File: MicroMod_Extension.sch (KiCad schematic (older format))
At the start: 78 parts, among them J1 2199230-4, J2 XKB_U262-16XN-4BVC11, J3 RSP-122811-01, J4 Screw_Terminal_01x04, J5 Conn_01x08, J6 Conn_01x08, J7 Conn_01x02, J8 Conn_01x04, J9 Conn_01x04, SW1 TL1014BF160QG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

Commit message: update pcb
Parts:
- removed J7: Conn_01x02, Connector_PinHeader_2.54mm:PinHeader_1x02_P2.54mm_Vertical, symbol Connector_Generic:Conn_01x02
- added J7: Conn_01x04, Connector_JST:JST_SUR_SM04B-SURS-TF_1x04-1MP_P0.80mm_Horizontal, symbol Connector_Generic:Conn_01x04
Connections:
- net GND: now also J7.4 (Pin_4)
- net NRF_TX2: now reaches U2.17 (P0.11)
- net NRF_TX2: now also J7.3 (Pin_3)
- net NRF_RX2: now reaches U2.18 (P0.12)
- net NRF_RX2: now also J7.2 (Pin_2)
- no-connect marks 41 -> 40
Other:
- moved on the sheet: J4, J6, J8, J9
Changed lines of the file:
@@
 Wire Wire Line
 	11250 5325 11250 5225
-NoConn ~ 12050 3025
-NoConn ~ 12050 3125
 NoConn ~ 12050 2725
 NoConn ~ 12050 2825
@@
 $EndComp
 $Comp
-L Connector:Screw_Terminal_01x04 J4
-U 1 1 6180CF84
-P 15425 5275
-F 0 "J4" H 15505 5267 50  0000 L CNN
-F 1 "Screw_Terminal_01x04" H 15505 5176 50  0000 L CNN
-F 2 "Connector_JST:JST_SUR_SM04B-SURS-TF_1x04-1MP_P0.80mm_Horizontal" H 15425 5275 50  0001 C CNN
-F 3 "~" H 15425 5275 50  0001 C CNN
-	1    15425 5275
-	1    0    0    -1
-$EndComp
-Text Label 15225 5275 2    50   ~ 0
-NRF_SWCLK
-Text Label 15225 5375 2    50   ~ 0
-NRF_SWIO
-Text Label 15225 5175 2    50   ~ 0
-VCC_NRF
-$Comp
-L power:GND #PWR0133
-U 1 1 61871AB2
-P 15225 5475
-F 0 "#PWR0133" H 15225 5225 50  0001 C CNN
-F 1 "GND" V 15230 5347 50  0000 R CNN
-F 2 "" H 15225 5475 50  0001 C CNN
-F 3 "" H 15225 5475 50  0001 C CNN
-	1    15225 5475
-	0    1    1    0
-$EndComp
-$Comp
-L Connector_Generic:Conn_01x02 J7
-U 1 1 6189B41D
-P 15400 750
-F 0 "J7" H 15480 742 50  0000 L CNN
-F 1 "Conn_01x02" H 15480 651 50  0000 L CNN
-F 2 "Connector_PinHeader_2.54mm:PinHeader_1x02_P2.54mm_Vertical" H 15400 750 50  0001 C CNN
-F 3 "~" H 15400 750 50  0001 C CNN
-	1    15400 750
-	1    0    0    -1
-$EndComp
-$Comp
-L power:GND #PWR0134
-U 1 1 6189BE51
-P 15200 850
-F 0 "#PWR0134" H 15200 600 50  0001 C CNN
-F 1 "GND" V 15205 722 50  0000 R CNN
-F 2 "" H 15200 850 50  0001 C CNN
-F 3 "" H 15200 850 50  0001 C CNN
-	1    15200 850
-	0    1    1    0
-$EndComp
-Text GLabel 15200 750  0    50   Input ~ 0
-BATT
-$Comp
 L Connector_Generic:Conn_01x08 J5
 U 1 1 6197BE2D
@@
 L Connector_Generic:Conn_01x08 J6
 U 1 1 6197CCB9
-P 15425 3025
-F 0 "J6" H 15505 3017 50  0000 L CNN
-F 1 "Conn_01x08" H 15505 2926 50  0000 L CNN
-F 2 "Connector_JST:JST_SUR_BM08B-SURS-TF_1x08-1MP_P0.80mm_Vertical" H 15425 3025 50  0001 C CNN
-F 3 "~" H 15425 3025 50  0001 C CNN
-	1    15425 3025
-	1    0    0    -1
-$EndComp
-Text Label 15225 2725 2    50   ~ 0
+P 14325 2000
+F 0 "J6" H 14405 1992 50  0000 L CNN
+F 1 "Conn_01x08" H 14405 1901 50  0000 L CNN
+F 2 "Connector_JST:JST_SUR_BM08B-SURS-TF_1x08-1MP_P0.80mm_Vertical" H 14325 2000 50  0001 C CNN
+F 3 "~" H 14325 2000 50  0001 C CNN
+	1    14325 2000
+	1    0    0    -1
+$EndComp
+Text Label 14125 1700 2    50   ~ 0
 VCC
 $Comp
@@
 L power:GND #PWR0136
 U 1 1 61A085B5
-P 15225 3425
-F 0 "#PWR0136" H 15225 3175 50  0001 C CNN
-F 1 "GND" V 15230 3297 50  0000 R CNN
-F 2 "" H 15225 3425 50  0001 C CNN
-F 3 "" H 15225 3425 50  0001 C CNN
-	1    15225 3425
+P 14125 2400
+F 0 "#PWR0136" H 14125 2150 50  0001 C CNN
+F 1 "GND" V 14130 2272 50  0000 R CNN
+F 2 "" H 14125 2400 50  0001 C CNN
+F 3 "" H 14125 2400 50  0001 C CNN
+	1    14125 2400
 	0    1    1    0
 $EndComp
@@
 Text Label 15225 2175 2    50   ~ 0
 MOTOR4
-Text Label 15225 2825 2    50   ~ 0
+Text Label 14125 1800 2    50   ~ 0
 E_SDA
-Text Label 15225 2925 2    50   ~ 0
+Text Label 14125 1900 2    50   ~ 0
 E_SCL
-Text Label 15225 3025 2    50   ~ 0
+Text Label 14125 2000 2    50   ~ 0
 E_SPI_SCK
-Text Label 15225 3125 2    50   ~ 0
+Text Label 14125 2100 2    50   ~ 0
 E_SPI_MISO
-Text Label 15225 3225 2    50   ~ 0
+Text Label 14125 2200 2    50   ~ 0
 E_SPI_MOSI
-Text Label 15225 3325 2    50   ~ 0
+Text Label 14125 2300 2    50   ~ 0
 B4
 Text GLabel 15225 1675 0    50   Input ~ 0
@@
 	0    1    1    0
 $EndComp
-$Comp
-L Connector_Generic:Conn_01x04 J8
-U 1 1 61BEF3FE
-P 15425 3975
-F 0 "J8" H 15505 3967 50  0000 L CNN
-F 1 "Conn_01x04" H 15505 3876 50  0000 L CNN
-F 2 "Connector_JST:JST_SUR_SM04B-SURS-TF_1x04-1MP_P0.80mm_Horizontal" H 15425 3975 50  0001 C CNN
-F 3 "~" H 15425 3975 50  0001 C CNN
-	1    15425 3975
-	1    0    0    -1
-$EndComp
-$Comp
-L power:GND #PWR0138
-U 1 1 61BF109A
-P 15225 4175
-F 0 "#PWR0138" H 15225 3925 50  0001 C CNN
-F 1 "GND" V 15230 4047 50  0000 R CNN
-F 2 "" H 15225 4175 50  0001 C CNN
-F 3 "" H 15225 4175 50  0001 C CNN
-	1    15225 4175
-	0    1    1    0
-$EndComp
-Text Label 15225 3975 2    50   ~ 0
-E_RX1
-Text Label 15225 4075 2    50   ~ 0
-E_TX1
-$Comp
-L Connector_Generic:Conn_01x04 J9
-U 1 1 61C420AB
-P 15425 4625
-F 0 "J9" H 15505 4617 50  0000 L CNN
-F 1 "Conn_01x04" H 15505 4526 50  0000 L CNN
-F 2 "Connector_JST:JST_SUR_SM04B-SURS-TF_1x04-1MP_P0.80mm_Horizontal" H 15425 4625 50  0001 C CNN
-F 3 "~" H 15425 4625 50  0001 C CNN
-	1    15425 4625
-	1    0    0    -1
-$EndComp
-$Comp
-L power:GND #PWR0139
-U 1 1 61C420B1
-P 15225 4825
-F 0 "#PWR0139" H 15225 4575 50  0001 C CNN
-F 1 "GND" V 15230 4697 50  0000 R CNN
-F 2 "" H 15225 4825 50  0001 C CNN
-F 3 "" H 15225 4825 50  0001 C CNN
-	1    15225 4825
-	0    1    1    0
-$EndComp
-Text Label 15225 4625 2    50   ~ 0
-E_RX2
-Text Label 15225 4725 2    50   ~ 0
-E_TX2
-Wire Notes Line
-	14700 5650 14700 475
-Wire Notes Line
-	14700 5650 16050 5650
 Text Notes 14800 600  0    50   ~ 0
 Connector
@@
 	14775 1200 14925 1200
 Connection ~ 14925 1200
-NoConn ~ 15225 3875
-NoConn ~ 15225 4525
+Text Label 12050 3025 0    50   ~ 0
+NRF_TX2
+Text Label 12050 3125 0    50   ~ 0
+NRF_RX2
+NoConn ~ 14100 2700
+Text Label 14100 2900 2    50   ~ 0
+NRF_TX2
+Text Label 14100 2800 2    50   ~ 0
+NRF_RX2
+$Comp
+L power:GND #PWR0134
+U 1 1 61889B5C
+P 14100 3000
+F 0 "#PWR0134" H 14100 2750 50  0001 C CNN
+F 1 "GND" V 14105 2872 50  0000 R CNN
+F 2 "" H 14100 3000 50  0001 C CNN
+F 3 "" H 14100 3000 50  0001 C CNN
+	1    14100 3000
+	0    1    1    0
+$EndComp
+$Comp
+L Connector_Generic:Conn_01x04 J7
+U 1 1 61889B56
+P 14300 2800
+F 0 "J7" H 14380 2792 50  0000 L CNN
+F 1 "Conn_01x04" H 14380 2701 50  0000 L CNN
+F 2 "Connector_JST:JST_SUR_SM04B-SURS-TF_1x04-1MP_P0.80mm_Horizontal" H 14300 2800 50  0001 C CNN
+F 3 "~" H 14300 2800 50  0001 C CNN
+	1    14300 2800
+	1    0    0    -1
+$EndComp
+NoConn ~ 15050 3325
+NoConn ~ 15050 2675
+Text Label 15050 3525 2    50   ~ 0
+E_TX2
+Text Label 15050 3425 2    50   ~ 0
+E_RX2
+$Comp
+L power:GND #PWR0139
+U 1 1 61C420B1
+P 15050 3625
+F 0 "#PWR0139" H 15050 3375 50  0001 C CNN
+F 1 "GND" V 15055 3497 50  0000 R CNN
+F 2 "" H 15050 3625 50  0001 C CNN
+F 3 "" H 15050 3625 50  0001 C CNN
+	1    15050 3625
+	0    1    1    0
+$EndComp
+$Comp
+L Connector_Generic:Conn_01x04 J9
+U 1 1 61C420AB
+P 15250 3425
+F 0 "J9" H 15330 3417 50  0000 L CNN
+F 1 "Conn_01x04" H 15330 3326 50  0000 L CNN
+F 2 "Connector_JST:JST_SUR_SM04B-SURS-TF_1x04-1MP_P0.80mm_Horizontal" H 15250 3425 50  0001 C CNN
+F 3 "~" H 15250 3425 50  0001 C CNN
+	1    15250 3425
+	1    0    0    -1
+$EndComp
+Text Label 15050 2875 2    50   ~ 0
+E_TX1
+Text Label 15050 2775 2    50   ~ 0
+E_RX1
+$Comp
+L power:GND #PWR0138
+U 1 1 61BF109A
+P 15050 2975
+F 0 "#PWR0138" H 15050 2725 50  0001 C CNN
+F 1 "GND" V 15055 2847 50  0000 R CNN
+F 2 "" H 15050 2975 50  0001 C CNN
+F 3 "" H 15050 2975 50  0001 C CNN
+	1    15050 2975
+	0    1    1    0
+$EndComp
+$Comp
+L Connector_Generic:Conn_01x04 J8
+U 1 1 61BEF3FE
+P 15250 2775
+F 0 "J8" H 15330 2767 50  0000 L CNN
+F 1 "Conn_01x04" H 15330 2676 50  0000 L CNN
+F 2 "Connector_JST:JST_SUR_SM04B-SURS-TF_1x04-1MP_P0.80mm_Horizontal" H 15250 2775 50  0001 C CNN
+F 3 "~" H 15250 2775 50  0001 C CNN
+	1    15250 2775
+	1    0    0    -1
+$EndComp
+$Comp
+L power:GND #PWR0133
+U 1 1 61871AB2
+P 14125 3625
+F 0 "#PWR0133" H 14125 3375 50  0001 C CNN
+F 1 "GND" V 14130 3497 50  0000 R CNN
+F 2 "" H 14125 3625 50  0001 C CNN
+F 3 "" H 14125 3625 50  0001 C CNN
+	1    14125 3625
+	0    1    1    0
+$EndComp
+Text Label 14125 3325 2    50   ~ 0
+VCC_NRF
+Text Label 14125 3525 2    50   ~ 0
+NRF_SWIO
+Text Label 14125 3425 2    50   ~ 0
+NRF_SWCLK
+$Comp
+L Connector:Screw_Terminal_01x04 J4
+U 1 1 6180CF84
+P 14325 3425
+F 0 "J4" H 14405 3417 50  0000 L CNN
+F 1 "Screw_Terminal_01x04" H 14405 3326 50  0000 L CNN
+F 2 "Connector_JST:JST_SUR_SM04B-SURS-TF_1x04-1MP_P0.80mm_Horizontal" H 14325 3425 50  0001 C CNN
+F 3 "~" H 14325 3425 50  0001 C CNN
+	1    14325 3425
+	1    0    0    -1
+$EndComp
 $EndSCHEMATC

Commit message: finish version 1.0
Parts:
- added J10: Conn_01x02, MicroMod_Extension:BATTARY, symbol Connector_Generic:Conn_01x02
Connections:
- net BATT: now also J10.1 (Pin_1)
- net GND: now also J10.2 (Pin_2)
- net at FL2.2 (OUT/IN): now also C11.2; no longer J3.1
- net at FL3.2 (OUT/IN): now also J3.1; no longer C11.2
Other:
- moved on the sheet: C11, E1, J3, L1, L3
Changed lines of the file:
@@
 L MicroMod_Extension:RSP-122811-01 J3
 U 1 1 617ED359
-P 4200 1550
-F 0 "J3" H 4192 1857 50  0000 C CNN
-F 1 "RSP-122811-01" H 4192 1766 50  0000 C CNN
-F 2 "MicroMod_Extension:SAMTEC_RSP-122811-01" H 4200 1550 50  0001 L BNN
-F 3 "" H 4200 1550 50  0001 L BNN
-F 4 "Samtec" H 4200 1550 50  0001 L BNN "MANUFACTURER"
-F 5 "H" H 4200 1550 50  0001 L BNN "PARTREV"
-F 6 "Manufacturer Recommendations" H 4200 1550 50  0001 L BNN "STANDARD"
-F 7 "1.44mm" H 4200 1550 50  0001 L BNN "MAXIMUM_PACKAGE_HEIGHT"
-	1    4200 1550
-	1    0    0    -1
-$EndComp
-Wire Wire Line
-	4300 1450 4600 1450
+P 4200 2675
+F 0 "J3" H 4192 2982 50  0000 C CNN
+F 1 "RSP-122811-01" H 4192 2891 50  0000 C CNN
+F 2 "MicroMod_Extension:SAMTEC_RSP-122811-01" H 4200 2675 50  0001 L BNN
+F 3 "" H 4200 2675 50  0001 L BNN
+F 4 "Samtec" H 4200 2675 50  0001 L BNN "MANUFACTURER"
+F 5 "H" H 4200 2675 50  0001 L BNN "PARTREV"
+F 6 "Manufacturer Recommendations" H 4200 2675 50  0001 L BNN "STANDARD"
+F 7 "1.44mm" H 4200 2675 50  0001 L BNN "MAXIMUM_PACKAGE_HEIGHT"
+	1    4200 2675
+	1    0    0    -1
+$EndComp
+Wire Wire Line
+	4300 2575 4600 2575
 $Comp
 L power:GND #PWR0119
 U 1 1 617F3384
-P 4300 1550
-F 0 "#PWR0119" H 4300 1300 50  0001 C CNN
-F 1 "GND" V 4305 1422 50  0000 R CNN
-F 2 "" H 4300 1550 50  0001 C CNN
-F 3 "" H 4300 1550 50  0001 C CNN
-	1    4300 1550
+P 4300 2675
+F 0 "#PWR0119" H 4300 2425 50  0001 C CNN
+F 1 "GND" V 4305 2547 50  0000 R CNN
+F 2 "" H 4300 2675 50  0001 C CNN
+F 3 "" H 4300 2675 50  0001 C CNN
+	1    4300 2675
 	0    -1   -1   0
 $EndComp
@@
 L Device:C C11
 U 1 1 6180E811
-P 4450 2575
-F 0 "C11" H 4565 2621 50  0000 L CNN
-F 1 "2.5p" H 4565 2530 50  0000 L CNN
-F 2 "Capacitor_SMD:C_0402_1005Metric" H 4488 2425 50  0001 C CNN
-F 3 "~" H 4450 2575 50  0001 C CNN
-	1    4450 2575
+P 4450 1450
+F 0 "C11" H 4565 1496 50  0000 L CNN
+F 1 "2.5p" H 4565 1405 50  0000 L CNN
+F 2 "Capacitor_SMD:C_0402_1005Metric" H 4488 1300 50  0001 C CNN
+F 3 "~" H 4450 1450 50  0001 C CNN
+	1    4450 1450
 	0    -1   -1   0
 $EndComp
@@
 L Device:L L3
 U 1 1 61810D4B
-P 4200 2825
-F 0 "L3" H 4253 2871 50  0000 L CNN
-F 1 "1nH" H 4253 2780 50  0000 L CNN
-F 2 "Inductor_SMD:L_0402_1005Metric" H 4200 2825 50  0001 C CNN
-F 3 "~" H 4200 2825 50  0001 C CNN
-	1    4200 2825
+P 4200 1700
+F 0 "L3" H 4253 1746 50  0000 L CNN
+F 1 "1nH" H 4253 1655 50  0000 L CNN
+F 2 "Inductor_SMD:L_0402_1005Metric" H 4200 1700 50  0001 C CNN
+F 3 "~" H 4200 1700 50  0001 C CNN
+	1    4200 1700
 	1    0    0    -1
 $EndComp
@@
 L Device:L L1
 U 1 1 61813241
-P 3950 2575
-F 0 "L1" V 4140 2575 50  0000 C CNN
-F 1 "4.7nH" V 4049 2575 50  0000 C CNN
-F 2 "Inductor_SMD:L_0402_1005Metric" H 3950 2575 50  0001 C CNN
-F 3 "~" H 3950 2575 50  0001 C CNN
-	1    3950 2575
+P 3950 1450
+F 0 "L1" V 4140 1450 50  0000 C CNN
+F 1 "4.7nH" V 4049 1450 50  0000 C CNN
+F 2 "Inductor_SMD:L_0402_1005Metric" H 3950 1450 50  0001 C CNN
+F 3 "~" H 3950 1450 50  0001 C CNN
+	1    3950 1450
 	0    -1   -1   0
 $EndComp
 Wire Wire Line
-	4100 2575 4200 2575
-Wire Wire Line
-	4200 2575 4200 2675
-Wire Wire Line
-	4200 2575 4300 2575
-Connection ~ 4200 2575
-Wire Wire Line
-	4200 2975 4200 3075
+	4100 1450 4200 1450
+Wire Wire Line
+	4200 1450 4200 1550
+Wire Wire Line
+	4200 1450 4300 1450
+Connection ~ 4200 1450
+Wire Wire Line
+	4200 1850 4200 1950
 $Comp
 L power:GND #PWR0121
 U 1 1 6181C983
-P 4200 3075
-F 0 "#PWR0121" H 4200 2825 50  0001 C CNN
-F 1 "GND" V 4205 2947 50  0000 R CNN
-F 2 "" H 4200 3075 50  0001 C CNN
-F 3 "" H 4200 3075 50  0001 C CNN
-	1    4200 3075
+P 4200 1950
+F 0 "#PWR0121" H 4200 1700 50  0001 C CNN
+F 1 "GND" V 4205 1822 50  0000 R CNN
+F 2 "" H 4200 1950 50  0001 C CNN
+F 3 "" H 4200 1950 50  0001 C CNN
+	1    4200 1950
 	1    0    0    -1
 $EndComp
@@
 L MicroMod_Extension:2450AT18B100E E1
 U 1 1 61821C76
-P 3725 2300
-F 0 "E1" H 3850 2397 50  0000 L CNN
-F 1 "2450AT18B100E" H 3850 2306 50  0000 L CNN
-F 2 "MicroMod_Extension:XDCR_2450AT18B100E" H 3725 2300 50  0001 L BNN
-F 3 "" H 3725 2300 50  0001 L BNN
-F 4 "Manufacturer Recommendation" H 3725 2300 50  0001 L BNN "STANDARD"
-F 5 "4.0" H 3725 2300 50  0001 L BNN "PARTREV"
-F 6 "Johanson Technology" H 3725 2300 50  0001 L BNN "MANUFACTURER"
-F 7 "1.4 mm" H 3725 2300 50  0001 L BNN "MAXIMUM_PACKAGE_HEIGHT"
-	1    3725 2300
-	1    0    0    -1
-$EndComp
-Wire Wire Line
-	3725 2500 3725 2575
-Wire Wire Line
-	3725 2575 3800 2575
+P 3725 1175
+F 0 "E1" H 3850 1272 50  0000 L CNN
+F 1 "2450AT18B100E" H 3850 1181 50  0000 L CNN
+F 2 "MicroMod_Extension:XDCR_2450AT18B100E" H 3725 1175 50  0001 L BNN
+F 3 "" H 3725 1175 50  0001 L BNN
+F 4 "Manufacturer Recommendation" H 3725 1175 50  0001 L BNN "STANDARD"
+F 5 "4.0" H 3725 1175 50  0001 L BNN "PARTREV"
+F 6 "Johanson Technology" H 3725 1175 50  0001 L BNN "MANUFACTURER"
+F 7 "1.4 mm" H 3725 1175 50  0001 L BNN "MAXIMUM_PACKAGE_HEIGHT"
+	1    3725 1175
+	1    0    0    -1
+$EndComp
+Wire Wire Line
+	3725 1375 3725 1450
+Wire Wire Line
+	3725 1450 3800 1450
 Text Label 12050 3825 0    50   ~ 0
 PA_SW_ANT
@@
 	1    0    0    -1
 $EndComp
+$Comp
+L Connector_Generic:Conn_01x02 J10
+U 1 1 61893954
+P 15450 750
+F 0 "J10" H 15530 742 50  0000 L CNN
+F 1 "Conn_01x02" H 15530 651 50  0000 L CNN
+F 2 "MicroMod_Extension:BATTARY" H 15450 750 50  0001 C CNN
+F 3 "~" H 15450 750 50  0001 C CNN
+	1    15450 750
+	1    0    0    -1
+$EndComp
+$Comp
+L power:GND #PWR0141
+U 1 1 61894E7F
+P 15250 850
+F 0 "#PWR0141" H 15250 600 50  0001 C CNN
+F 1 "GND" V 15255 722 50  0000 R CNN
+F 2 "" H 15250 850 50  0001 C CNN
+F 3 "" H 15250 850 50  0001 C CNN
+	1    15250 850
+	0    1    1    0
+$EndComp
+Text GLabel 15250 750  0    50   Input ~ 0
+BATT
 $EndSCHEMATC

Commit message: update pcb
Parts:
- added J11: Screw_Terminal_01x04, Connector_JST:JST_SUR_SM04B-SURS-TF_1x04-1MP_P0.80mm_Horizontal, symbol Connector:Screw_Terminal_01x04
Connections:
- net GND: now also J11.4 (Pin_4)
- net STM_SWCLK: now also J11.2 (Pin_2)
- net STM_SWIO: now also J11.3 (Pin_3)
- net VCC: now also J11.1 (Pin_1)
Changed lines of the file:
@@
 Text GLabel 15250 750  0    50   Input ~ 0
 BATT
+$Comp
+L power:GND #PWR0142
+U 1 1 619F1B8D
+P 14125 4275
+F 0 "#PWR0142" H 14125 4025 50  0001 C CNN
+F 1 "GND" V 14130 4147 50  0000 R CNN
+F 2 "" H 14125 4275 50  0001 C CNN
+F 3 "" H 14125 4275 50  0001 C CNN
+	1    14125 4275
+	0    1    1    0
+$EndComp
+Text Label 14125 3975 2    50   ~ 0
+VCC
+Text Label 14125 4175 2    50   ~ 0
+STM_SWIO
+Text Label 14125 4075 2    50   ~ 0
+STM_SWCLK
+$Comp
+L Connector:Screw_Terminal_01x04 J11
+U 1 1 619F1B96
+P 14325 4075
+F 0 "J11" H 14405 4067 50  0000 L CNN
+F 1 "Screw_Terminal_01x04" H 14405 3976 50  0000 L CNN
+F 2 "Connector_JST:JST_SUR_SM04B-SURS-TF_1x04-1MP_P0.80mm_Horizontal" H 14325 4075 50  0001 C CNN
+F 3 "~" H 14325 4075 50  0001 C CNN
+	1    14325 4075
+	1    0    0    -1
+$EndComp
 $EndSCHEMATC

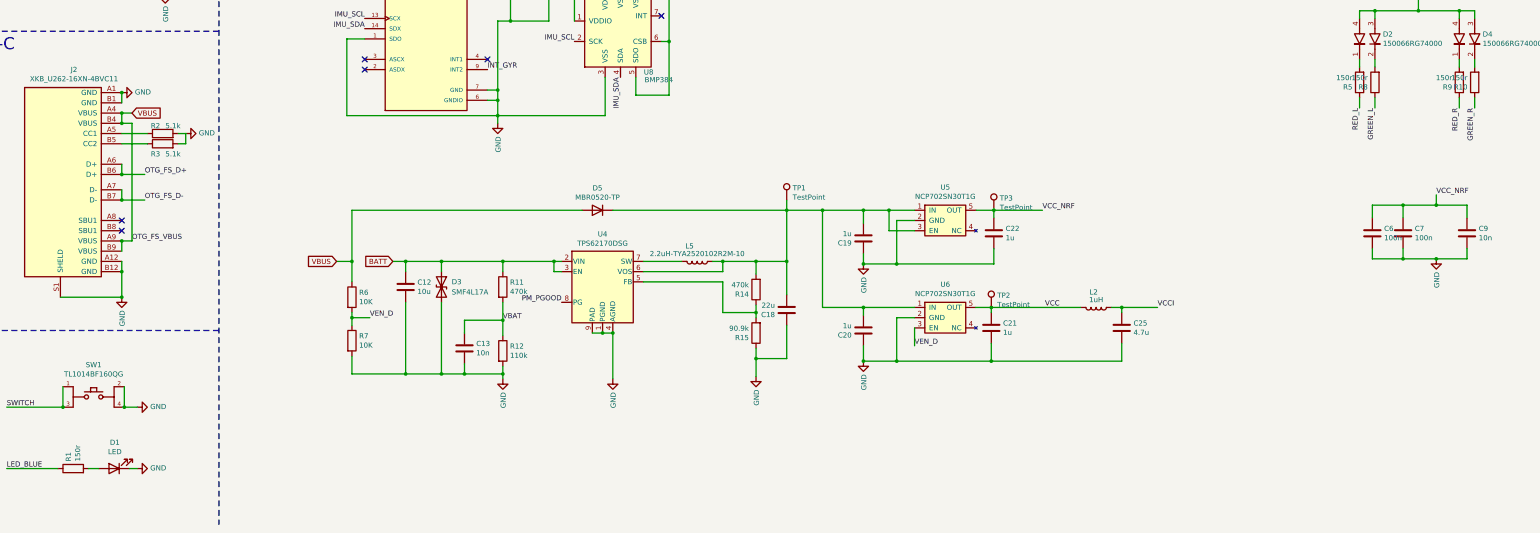
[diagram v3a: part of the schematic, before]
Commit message: fix led resistance
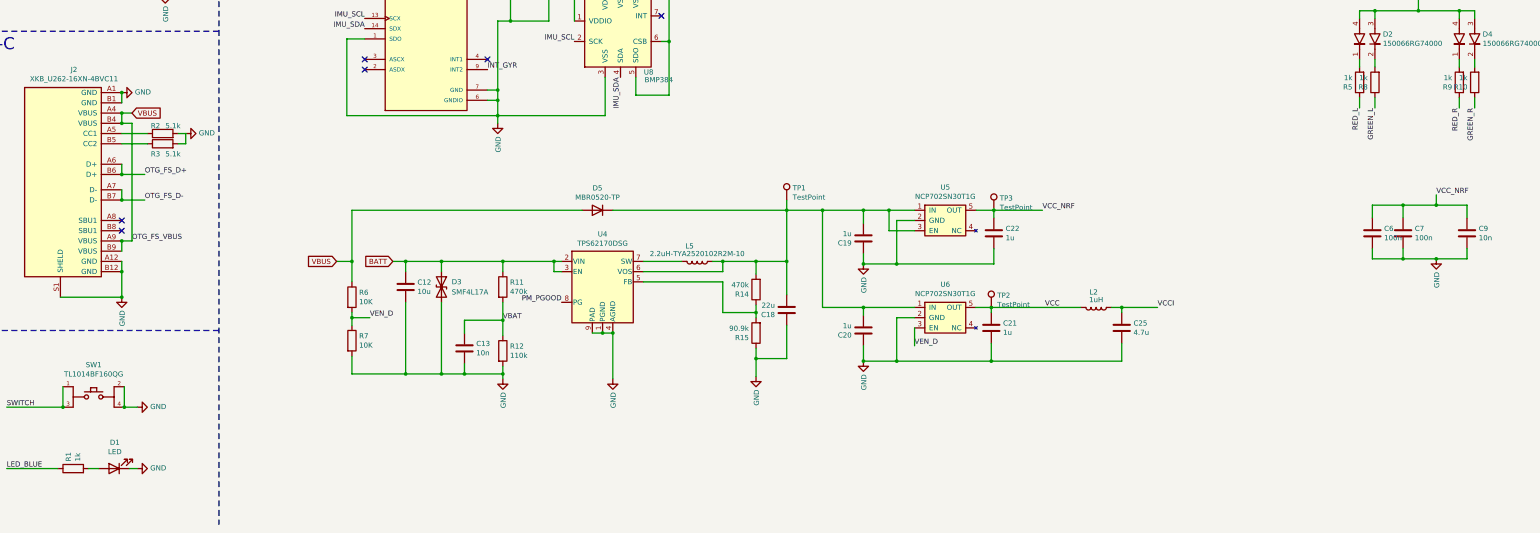
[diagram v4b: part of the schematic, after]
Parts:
- R1, R10, R5, R8, R9: value 150r -> 1k
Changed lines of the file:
@@
 P 1575 10675
 F 0 "R1" H 1645 10721 50  0000 L CNN
-F 1 "150r" H 1645 10630 50  0000 L CNN
+F 1 "1k" H 1645 10630 50  0000 L CNN
 F 2 "Resistor_SMD:R_0402_1005Metric" V 1505 10675 50  0001 C CNN
 F 3 "~" H 1575 10675 50  0001 C CNN
@@
 P 14150 6900
 F 0 "R5" H 14220 6946 50  0000 L CNN
-F 1 "150r" H 14220 6855 50  0000 L CNN
+F 1 "1k" H 14220 6855 50  0000 L CNN
 F 2 "Resistor_SMD:R_0402_1005Metric" V 14080 6900 50  0001 C CNN
 F 3 "~" H 14150 6900 50  0001 C CNN
@@
 P 14300 6900
 F 0 "R8" H 14370 6946 50  0000 L CNN
-F 1 "150r" H 14370 6855 50  0000 L CNN
+F 1 "1k" H 14370 6855 50  0000 L CNN
 F 2 "Resistor_SMD:R_0402_1005Metric" V 14230 6900 50  0001 C CNN
 F 3 "~" H 14300 6900 50  0001 C CNN
@@
 P 15125 6900
 F 0 "R9" H 15195 6946 50  0000 L CNN
-F 1 "150r" H 15195 6855 50  0000 L CNN
+F 1 "1k" H 15195 6855 50  0000 L CNN
 F 2 "Resistor_SMD:R_0402_1005Metric" V 15055 6900 50  0001 C CNN
 F 3 "~" H 15125 6900 50  0001 C CNN
@@
 P 15275 6900
 F 0 "R10" H 15345 6946 50  0000 L CNN
-F 1 "150r" H 15345 6855 50  0000 L CNN
+F 1 "1k" H 15345 6855 50  0000 L CNN
 F 2 "Resistor_SMD:R_0402_1005Metric" V 15205 6900 50  0001 C CNN
 F 3 "~" H 15275 6900 50  0001 C CNN
